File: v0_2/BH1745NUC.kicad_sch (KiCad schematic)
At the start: 1 part, among them IC4 BH1745NUC-E2

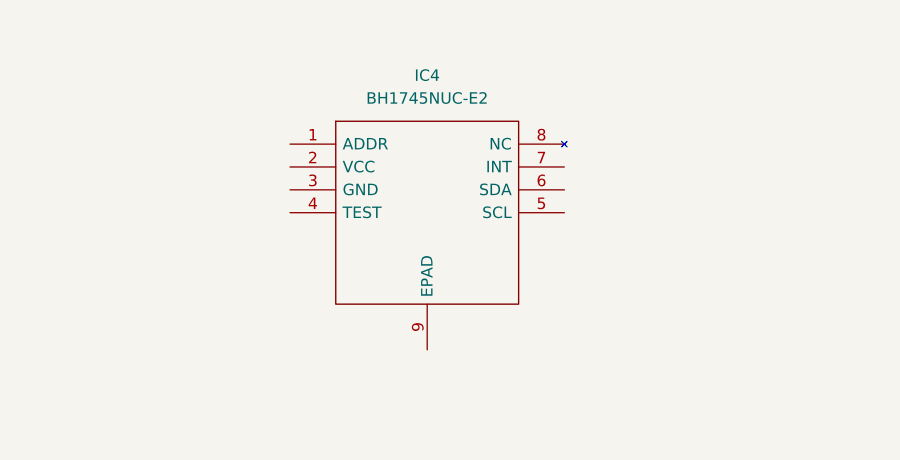
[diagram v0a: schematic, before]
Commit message: add sensor schematic
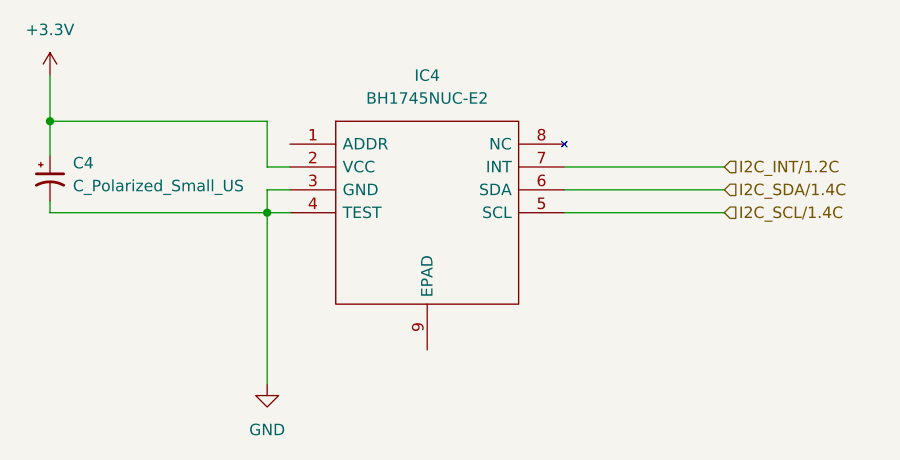
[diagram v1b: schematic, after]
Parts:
- added C4: C_Polarized_Small_US, symbol Device:C_Polarized_Small_US
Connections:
- net +3.3V: now reaches IC4.2 (VCC)
- net +3.3V: now also C4.1
- net GND: now reaches IC4.3 (GND)
- net GND: now also IC4.4 (TEST), C4.2
- net I2C_SCL/1.4C: now reaches IC4.5 (SCL)
- net I2C_SDA/1.4C: now reaches IC4.6 (SDA)
- net I2C_INT/1.2C: now reaches IC4.7 (INT)
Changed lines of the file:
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@@
 (kicad_sch (version 20230121) (generator eeschema)
   (paper "A4")
+  (junction (at 102.87 86.36) (diameter 0) (color 0 0 0 0)
+  )
+  (junction (at 127 96.52) (diameter 0) (color 0 0 0 0)
+  )
+  (wire (pts (xy 160.02 96.52) (xy 177.8 96.52))
+    (stroke (width 0) (type default))
+  )
+  (wire (pts (xy 127 91.44) (xy 127 86.36))
+    (stroke (width 0) (type default))
+  )
+  (wire (pts (xy 127 96.52) (xy 127 115.57))
+    (stroke (width 0) (type default))
+  )
+  (wire (pts (xy 102.87 86.36) (xy 102.87 90.17))
+    (stroke (width 0) (type default))
+  )
+  (wire (pts (xy 102.87 96.52) (xy 102.87 95.25))
+    (stroke (width 0) (type default))
+  )
+  (wire (pts (xy 127 86.36) (xy 102.87 86.36))
+    (stroke (width 0) (type default))
+  )
+  (wire (pts (xy 129.54 91.44) (xy 127 91.44))
+    (stroke (width 0) (type default))
+  )
+  (wire (pts (xy 127 93.98) (xy 127 96.52))
+    (stroke (width 0) (type default))
+  )
+  (wire (pts (xy 160.02 93.98) (xy 177.8 93.98))
+    (stroke (width 0) (type default))
+  )
+  (wire (pts (xy 160.02 91.44) (xy 177.8 91.44))
+    (stroke (width 0) (type default))
+  )
+  (wire (pts (xy 102.87 81.28) (xy 102.87 86.36))
+    (stroke (width 0) (type default))
+  )
+  (wire (pts (xy 129.54 93.98) (xy 127 93.98))
+    (stroke (width 0) (type default))
+  )
+  (wire (pts (xy 127 96.52) (xy 102.87 96.52))
+    (stroke (width 0) (type default))
+  )
+  (wire (pts (xy 129.54 96.52) (xy 127 96.52))
+    (stroke (width 0) (type default))
+  )
+  (hierarchical_label "I2C_SDA{slash}1.4C" (shape input) (at 177.8 93.98 0) (fields_autoplaced)
+    (effects (font (size 1.27 1.27)) (justify left))
+  )
+  (hierarchical_label "I2C_SCL{slash}1.4C" (shape input) (at 177.8 96.52 0) (fields_autoplaced)
+    (effects (font (size 1.27 1.27)) (justify left))
+  )
+  (hierarchical_label "I2C_INT{slash}1.2C" (shape input) (at 177.8 91.44 0) (fields_autoplaced)
+    (effects (font (size 1.27 1.27)) (justify left))
+  )
+  (symbol (lib_id "power:GND") (at 127 115.57 0) (unit 1)
+    (in_bom yes) (on_board yes) (dnp no) (fields_autoplaced)
+    (property "Reference" "#PWR019" (at 127 121.92 0)
+      (effects (font (size 1.27 1.27)) hide)
+    )
+    (property "Value" "GND" (at 127 120.65 0)
+      (effects (font (size 1.27 1.27)))
+    )
+    (property "Footprint" "" (at 127 115.57 0)
+      (effects (font (size 1.27 1.27)) hide)
+    )
+    (property "Datasheet" "" (at 127 115.57 0)
+      (effects (font (size 1.27 1.27)) hide)
+    )
+    (pin "1")
+    (instances
+      (project "v0_2"
+        (path "/678523e5-508b-4706-b0e0-f17e466a8d09/b4cf97a4-fc8e-43ca-87b5-9f012553953c"
+          (reference "#PWR019") (unit 1)
+        )
+      )
+    )
+  )
   (symbol (lib_id "BH1745NUC-E2:BH1745NUC-E2") (at 129.54 88.9 0) (unit 1)
     (in_bom yes) (on_board yes) (dnp no) (fields_autoplaced)
@@
         )
       )
+    )
+  )
+  (symbol (lib_id "power:+3.3V") (at 102.87 81.28 0) (unit 1)
+    (in_bom yes) (on_board yes) (dnp no) (fields_autoplaced)
+    (property "Reference" "#PWR018" (at 102.87 85.09 0)
+      (effects (font (size 1.27 1.27)) hide)
+    )
+    (property "Value" "+3.3V" (at 102.87 76.2 0)
+      (effects (font (size 1.27 1.27)))
+    )
+    (property "Footprint" "" (at 102.87 81.28 0)
+      (effects (font (size 1.27 1.27)) hide)
+    )
+    (property "Datasheet" "" (at 102.87 81.28 0)
+      (effects (font (size 1.27 1.27)) hide)
+    )
+    (pin "1")
+    (instances
+      (project "v0_2"
+        (path "/678523e5-508b-4706-b0e0-f17e466a8d09/b4cf97a4-fc8e-43ca-87b5-9f012553953c"
+          (reference "#PWR018") (unit 1)
+        )
+      )
+    )
+  )
+  (symbol (lib_id "Device:C_Polarized_Small_US") (at 102.87 92.71 0) (unit 1)
+    (in_bom yes) (on_board yes) (dnp no) (fields_autoplaced)
+    (property "Reference" "C4" (at 105.41 91.0082 0)
+      (effects (font (size 1.27 1.27)) (justify left))
+    )
+    (property "Value" "C_Polarized_Small_US" (at 105.41 93.5482 0)
+      (effects (font (size 1.27 1.27)) (justify left))
+    )
+    (property "Footprint" "" (at 102.87 92.71 0)
+      (effects (font (size 1.27 1.27)) hide)
+    )
+    (property "Datasheet" "~" (at 102.87 92.71 0)
+      (effects (font (size 1.27 1.27)) hide)
+    )
+    (pin "1")
+    (pin "2")
+    (instances
+      (project "v0_2"
+        (path "/678523e5-508b-4706-b0e0-f17e466a8d09/b4cf97a4-fc8e-43ca-87b5-9f012553953c"
+          (reference "C4") (unit 1)
+        )
+      )
